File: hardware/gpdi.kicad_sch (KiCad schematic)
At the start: 9 parts, among them J1 GPDI_A, Q1 BSN20

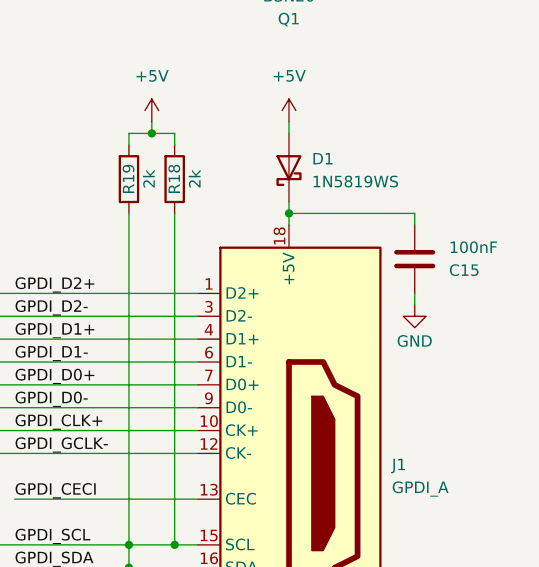
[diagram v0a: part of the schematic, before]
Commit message: Re-routed DDR3 on L4 & drew USB schematic
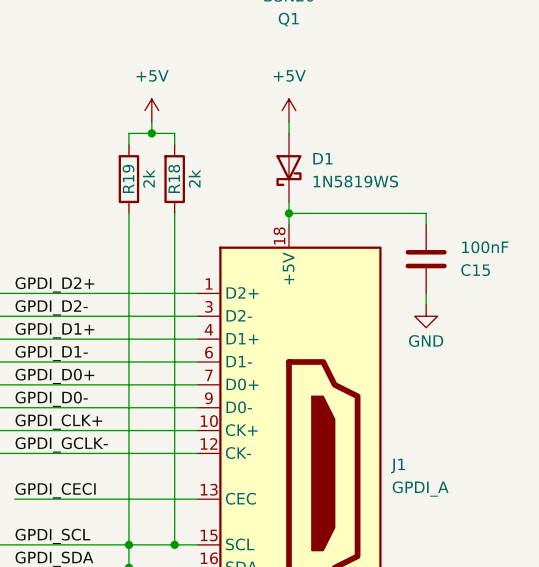
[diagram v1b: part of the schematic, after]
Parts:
- J1: LCSC Part # (none) -> C720616
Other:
- moved on the sheet: C15
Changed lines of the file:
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@@
 	(wire
 		(pts
-			(xy 144.78 81.28) (xy 158.75 81.28)
+			(xy 144.78 81.28) (xy 160.02 81.28)
 		)
 		(stroke
@@
 	(wire
 		(pts
-			(xy 158.75 81.28) (xy 158.75 82.55)
+			(xy 160.02 81.28) (xy 160.02 82.55)
 		)
 		(stroke
@@
 	(wire
 		(pts
-			(xy 158.75 90.17) (xy 158.75 91.44)
+			(xy 160.02 90.17) (xy 160.02 91.44)
 		)
 		(stroke
@@
 	(symbol
 		(lib_id "Device:C")
-		(at 158.75 86.36 0)
+		(at 160.02 86.36 0)
 		(mirror x)
 		(unit 1)
@@
 		(dnp no)
 		(property "Reference" "C15"
-			(at 162.56 87.6301 0)
+			(at 163.83 87.6301 0)
 			(effects
 				(font
@@
 		)
 		(property "Value" "100nF"
-			(at 162.56 85.0901 0)
+			(at 163.83 85.0901 0)
 			(effects
 				(font
@@
 		)
 		(property "Footprint" "Capacitor_SMD:C_0402_1005Metric"
-			(at 159.7152 82.55 0)
+			(at 160.9852 82.55 0)
 			(effects
 				(font
@@
 		)
 		(property "Datasheet" "~"
-			(at 158.75 86.36 0)
+			(at 160.02 86.36 0)
 			(effects
 				(font
@@
 		)
 		(property "Description" "Unpolarized capacitor"
-			(at 158.75 86.36 0)
+			(at 160.02 86.36 0)
 			(effects
 				(font
@@
 	(symbol
 		(lib_id "power:GND")
-		(at 158.75 91.44 0)
+		(at 160.02 91.44 0)
 		(mirror y)
 		(unit 1)
@@
 		(dnp no)
 		(property "Reference" "#PWR030"
-			(at 158.75 97.79 0)
+			(at 160.02 97.79 0)
 			(effects
 				(font
@@
 		)
 		(property "Value" "GND"
-			(at 158.75 95.504 0)
+			(at 160.02 95.504 0)
 			(effects
 				(font
@@
 		)
 		(property "Footprint" ""
-			(at 158.75 91.44 0)
+			(at 160.02 91.44 0)
 			(effects
 				(font
@@
 		)
 		(property "Datasheet" ""
-			(at 158.75 91.44 0)
+			(at 160.02 91.44 0)
 			(effects
 				(font
@@
 		)
 		(property "Description" "Power symbol creates a global label with name \"GND\" , ground"
-			(at 158.75 91.44 0)
+			(at 160.02 91.44 0)
 			(effects
 				(font
@@
 			(at 144.78 110.49 0)
 			(effects
+				(font
+					(size 1.27 1.27)
+				)
+				(hide yes)
+			)
+		)
+		(property "LCSC Part #" "C720616"
+			(at 144.78 110.49 0)
+			(effects
